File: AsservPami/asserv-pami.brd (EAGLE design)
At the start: 69.5 x 81.3 mm, 31 parts, among them IC1 NUCLEO-G431KB, IC2 7805TV

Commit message: ajout BAU et Voltmetre + label
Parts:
- added BAU, VOLTMETRE: 22-23-2021, con-molex:22-23-2021
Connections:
- new net N$7: BATTERIE.2, BAU.1
- net GND: now also VOLTMETRE.1
- net VIN: now also BAU.2, VOLTMETRE.2; no longer BATTERIE.2
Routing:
- net VIN: track 57.2 -> 66.7 mm
- net N$7: track 0.00 -> 8.67 mm
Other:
- board text added: "Alim"
- board text added: "BAU"
- board text added: "Codeur1"
- board text added: "Codeur2"
- board text added: "Couleur"
- board text added: "GPIO1"
- board text added: "GPIO2"
- board text added: "I2C"
- board text added: "Moteur1"
- board text added: "Moteur2"
- board text added: "Servo1"
- board text added: "Servo2"
- board text added: "StepUp"
- board text added: "Tirette"
- board text added: "UART"
- board text added: "USB DEBUG"
- board text added: "Volt"
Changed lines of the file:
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@@
 <hole x="29.21" y="3.81" drill="3"/>
 <hole x="12.7" y="74.93" drill="3"/>
+<text x="63.5" y="57.15" size="1.016" layer="1">Alim</text>
+<text x="54.61" y="57.15" size="1.016" layer="1">BAU</text>
+<text x="46.99" y="57.15" size="1.016" layer="1">Volt</text>
+<text x="64.77" y="50.8" size="1.016" layer="1" rot="R90">Codeur1</text>
+<text x="55.88" y="50.8" size="1.016" layer="1" rot="R90">Codeur2</text>
+<text x="54.61" y="36.83" size="1.016" layer="1">StepUp</text>
+<text x="55.88" y="2.54" size="1.016" layer="1">Moteur1</text>
+<text x="36.83" y="2.54" size="1.016" layer="1">Moteur2</text>
+<text x="13.97" y="22.86" size="1.016" layer="1" rot="R90">Tirette</text>
+<text x="13.97" y="15.24" size="1.016" layer="1" rot="R90">Couleur</text>
+<text x="13.97" y="8.89" size="1.016" layer="1" rot="R90">GPIO1</text>
+<text x="13.97" y="2.54" size="1.016" layer="1" rot="R90">GPIO2</text>
+<text x="10.16" y="38.1" size="1.016" layer="1" rot="R180">UART</text>
+<text x="22.86" y="40.64" size="1.016" layer="1" rot="R270">Servo1</text>
+<text x="22.86" y="34.29" size="1.016" layer="1" rot="R270">Servo2</text>
+<text x="19.05" y="53.34" size="1.016" layer="1">I2C</text>
+<text x="54.61" y="78.74" size="1.016" layer="1">USB DEBUG</text>
 </plain>
 <attributes>
@@
 <attribute name="VALUE" x="53.848" y="39.116" size="1.27" layer="27" ratio="10"/>
 </element>
+<element name="BAU" library="con-molex" library_urn="urn:adsk.eagle:library:165" package="22-23-2021" value="22-23-2021" x="57.15" y="60.96" smashed="yes" rot="R90">
+<attribute name="MF" value="MOLEX" x="45.72" y="53.34" size="1.778" layer="27" rot="R90" display="off"/>
+<attribute name="MPN" value="22-23-2021" x="45.72" y="53.34" size="1.778" layer="27" rot="R90" display="off"/>
+<attribute name="NAME" x="53.34" y="58.42" size="1.016" layer="25" ratio="10" rot="R90"/>
+<attribute name="OC_FARNELL" value="1462926" x="45.72" y="53.34" size="1.778" layer="27" rot="R90" display="off"/>
+<attribute name="OC_NEWARK" value="25C3832" x="45.72" y="53.34" size="1.778" layer="27" rot="R90" display="off"/>
+<attribute name="VALUE" x="62.23" y="58.42" size="1.016" layer="27" ratio="10" rot="R90"/>
+</element>
+<element name="VOLTMETRE" library="con-molex" library_urn="urn:adsk.eagle:library:165" package="22-23-2021" value="22-23-2021" x="49.53" y="60.96" smashed="yes" rot="R90">
+<attribute name="MF" value="MOLEX" x="38.1" y="53.34" size="1.778" layer="27" rot="R90" display="off"/>
+<attribute name="MPN" value="22-23-2021" x="38.1" y="53.34" size="1.778" layer="27" rot="R90" display="off"/>
+<attribute name="NAME" x="45.72" y="58.42" size="1.016" layer="25" ratio="10" rot="R90"/>
+<attribute name="OC_FARNELL" value="1462926" x="38.1" y="53.34" size="1.778" layer="27" rot="R90" display="off"/>
+<attribute name="OC_NEWARK" value="25C3832" x="38.1" y="53.34" size="1.778" layer="27" rot="R90" display="off"/>
+<attribute name="VALUE" x="54.61" y="58.42" size="1.016" layer="27" ratio="10" rot="R90"/>
+</element>
 </elements>
 <signals>
@@
 <contactref element="IC2" pad="2"/>
 <contactref element="C2" pad="2"/>
-<contactref element="BATTERIE" pad="1"/>
 <contactref element="POLOLU-MP6550-1-2" pad="5"/>
 <contactref element="POLOLU-MP6550-2-2" pad="5"/>
@@
 <wire x1="57.15" y1="68.58" x2="57.15" y2="67.31" width="1.016" layer="1"/>
 <contactref element="C3" pad="1"/>
+<contactref element="BATTERIE" pad="1"/>
+<contactref element="VOLTMETRE" pad="1"/>
 </signal>
 <signal name="N$1">
@@
 </signal>
 <signal name="VIN">
-<contactref element="BATTERIE" pad="2"/>
 <contactref element="C1" pad="1"/>
 <contactref element="IC2" pad="1"/>
 <contactref element="POLOLU-U3V40F12" pad="4"/>
 <contactref element="POLOLU-U3V40F12" pad="5"/>
-<wire x1="54.61" y1="67.31" x2="54.61" y2="63.5" width="1.016" layer="16"/>
-<wire x1="54.61" y1="63.5" x2="55.88" y2="62.23" width="1.016" layer="16"/>
 <wire x1="60.96" y1="39.37" x2="58.42" y2="39.37" width="1.016" layer="16"/>
-<wire x1="55.88" y1="62.23" x2="64.77" y2="62.23" width="1.016" layer="16"/>
-<wire x1="64.77" y1="62.23" x2="66.04" y2="62.23" width="1.016" layer="16"/>
-<wire x1="66.04" y1="62.23" x2="67.31" y2="60.96" width="1.016" layer="16"/>
 <wire x1="67.31" y1="60.96" x2="67.31" y2="43.18" width="1.016" layer="16"/>
 <wire x1="62.23" y1="43.18" x2="60.96" y2="41.91" width="1.016" layer="16"/>
@@
 <contactref element="C3" pad="2"/>
 <wire x1="58.42" y1="39.37" x2="58.42" y2="41.91" width="1.016" layer="16"/>
+<contactref element="BAU" pad="2"/>
+<wire x1="57.15" y1="62.23" x2="59.69" y2="62.23" width="1" layer="16"/>
+<wire x1="59.69" y1="62.23" x2="62.23" y2="64.77" width="1" layer="16"/>
+<wire x1="62.23" y1="64.77" x2="66.04" y2="64.77" width="1" layer="16"/>
+<wire x1="66.04" y1="64.77" x2="67.31" y2="63.5" width="1" layer="16"/>
+<wire x1="67.31" y1="63.5" x2="67.31" y2="60.96" width="1" layer="16"/>
+<contactref element="VOLTMETRE" pad="2"/>
+<wire x1="57.15" y1="62.23" x2="54.61" y2="62.23" width="1" layer="16"/>
+<wire x1="54.61" y1="62.23" x2="49.53" y2="62.23" width="1" layer="16"/>
+<wire x1="54.61" y1="67.31" x2="54.61" y2="62.23" width="1" layer="16"/>
 </signal>
 <signal name="SDA">
@@
 <wire x1="8.89" y1="38.1" x2="8.89" y2="35.56" width="1.016" layer="16"/>
 </signal>
+<signal name="N$7">
+<contactref element="BATTERIE" pad="2"/>
+<contactref element="BAU" pad="1"/>
+<wire x1="57.15" y1="59.69" x2="59.69" y2="59.69" width="1" layer="16"/>
+<wire x1="59.69" y1="59.69" x2="62.23" y2="62.23" width="1" layer="16"/>
+<wire x1="62.23" y1="62.23" x2="64.77" y2="62.23" width="1" layer="16"/>
+</signal>
 </signals>

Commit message: for impression
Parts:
- moved TIRETTE 6.35 mm to (8.89, 31.8)
- moved UART 6.35 mm to (8.89, 40.6)
- moved COULEUR 5.08 mm to (8.89, 22.9)
- moved GPIO1 2.54 mm to (8.89, 14.0)
- moved C1 2.54 mm to (52.1, 73.7)
- moved I2C 1.27 mm to (19.1, 44.5)
- moved SERVO2 1.27 mm to (21.6, 30.5)
- moved USB-DEBUG 1.27 mm to (53.3, 78.7)
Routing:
- net N$6: track 41.9 -> 35.3 mm
- net N$5: track 41.7 -> 36.8 mm
- net TIRETTE: track 62.5 -> 58.1 mm
- net COULEUR: track 66.4 -> 63.9 mm
- net SERVO1: track 35.1 -> 36.6 mm
- net SCL: track 29.0 -> 30.3 mm
- net USB-D+: track 44.7 -> 43.4 mm
- net SERVO2: track 39.7 -> 40.9 mm
- net SDA: track 35.9 -> 37.1 mm
- net GND: track 1.27 -> 0.00 mm
- net VIN: track 66.7 -> 65.6 mm
- net GPIO1: track 69.9 -> 69.2 mm
- net 5V: track 178.1 -> 178.6 mm

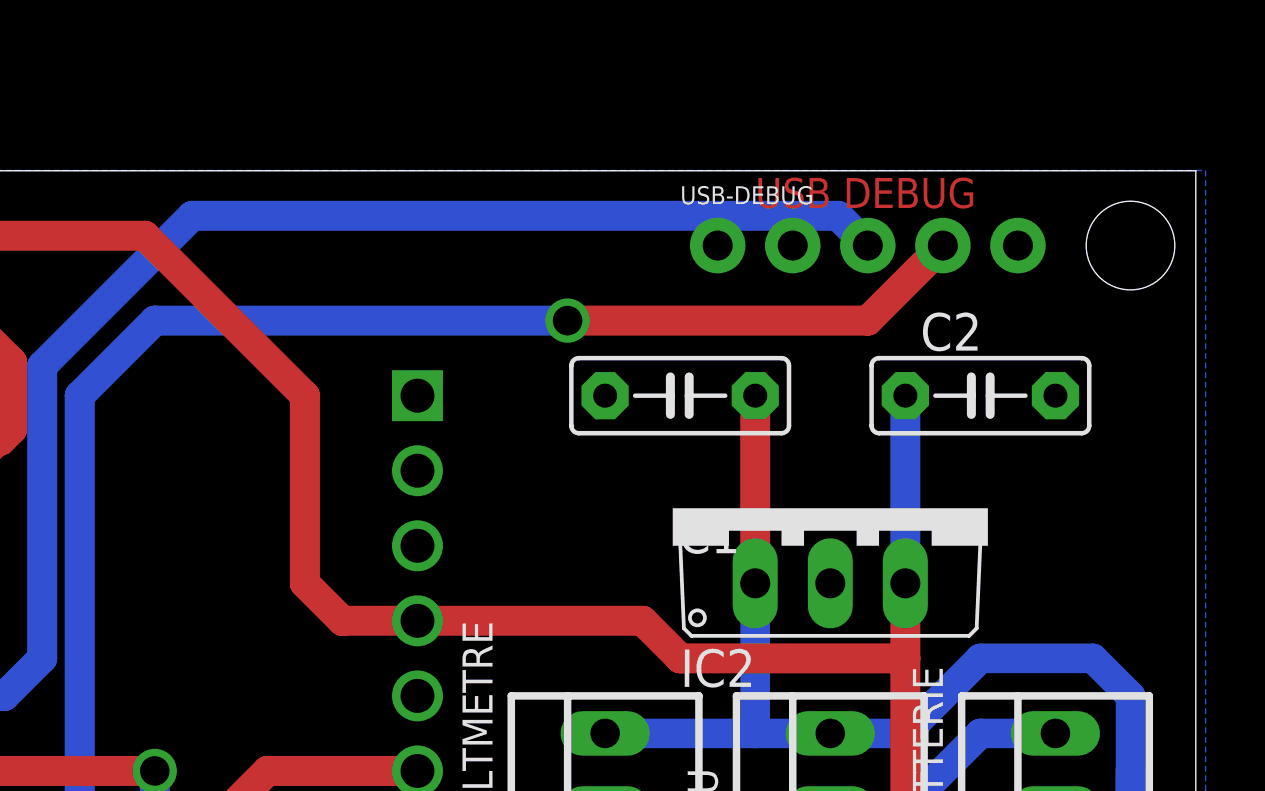
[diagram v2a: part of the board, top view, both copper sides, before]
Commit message: fix court circuit
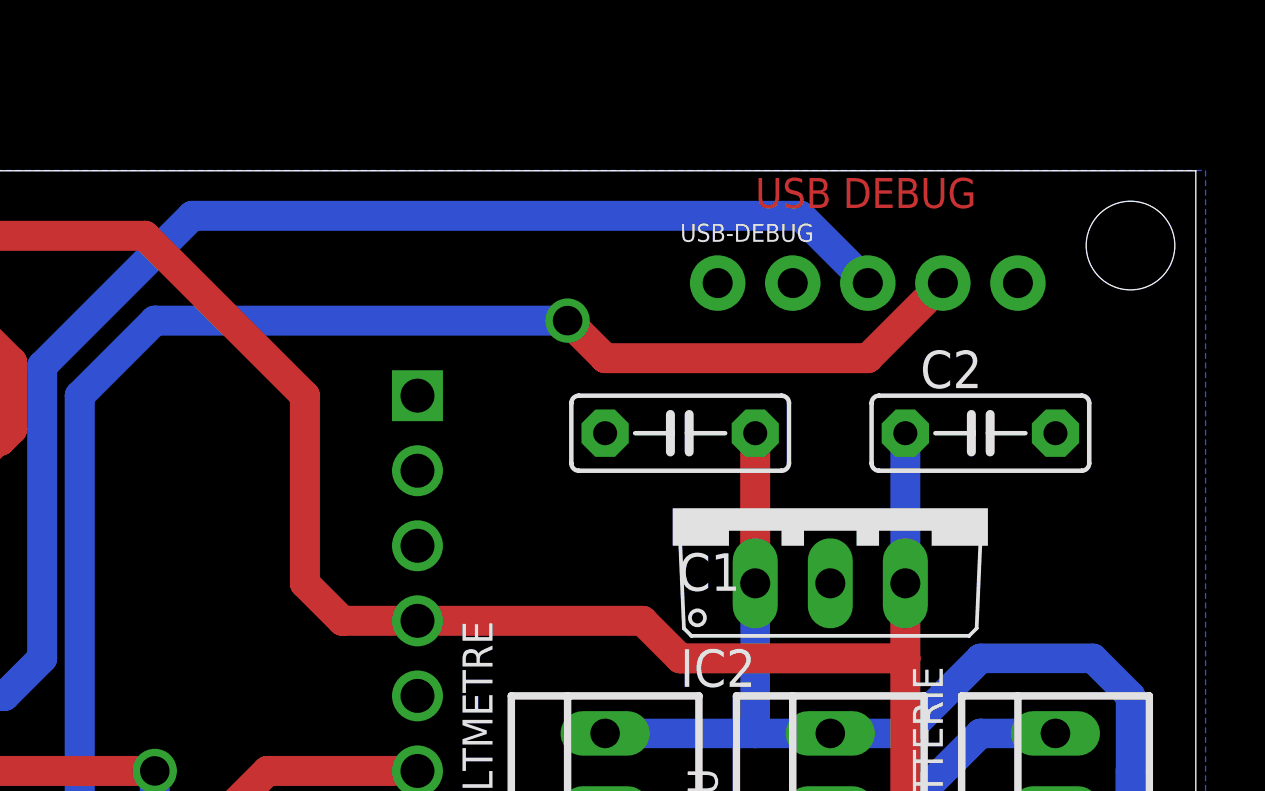
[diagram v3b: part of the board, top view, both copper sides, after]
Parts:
- moved C1 1.27 mm to (52.1, 72.4)
- moved C2 1.27 mm to (62.2, 72.4)
- moved USB-DEBUG 1.27 mm to (53.3, 77.5)
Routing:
- net 5V: track 178.6 -> 177.3 mm
- net VIN: track 65.6 -> 64.3 mm
- net USB-D-: track 64.9 -> 65.4 mm
- net USB-D+: track 43.4 -> 43.9 mm
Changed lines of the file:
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@@
 <attribute name="VALUE" x="69.85" y="58.42" size="1.016" layer="27" ratio="10" rot="R90"/>
 </element>
-<element name="C1" library="capacitor-wima" library_urn="urn:adsk.eagle:library:116" package="C5B2.5" value="0.33uF" x="52.07" y="73.66" smashed="yes" rot="R180">
-<attribute name="NAME" x="54.102" y="69.596" size="1.27" layer="25" ratio="10" rot="R180"/>
-<attribute name="VALUE" x="54.102" y="76.454" size="1.27" layer="27" ratio="10" rot="R180"/>
-</element>
-<element name="C2" library="capacitor-wima" library_urn="urn:adsk.eagle:library:116" package="C5B2.5" value="0.1uF" x="62.23" y="73.66" smashed="yes">
-<attribute name="NAME" x="60.198" y="75.184" size="1.27" layer="25" ratio="10"/>
-<attribute name="VALUE" x="60.198" y="70.866" size="1.27" layer="27" ratio="10"/>
+<element name="C1" library="capacitor-wima" library_urn="urn:adsk.eagle:library:116" package="C5B2.5" value="0.33uF" x="52.07" y="72.39" smashed="yes" rot="R180">
+<attribute name="NAME" x="54.102" y="68.326" size="1.27" layer="25" ratio="10" rot="R180"/>
+<attribute name="VALUE" x="54.102" y="75.184" size="1.27" layer="27" ratio="10" rot="R180"/>
+</element>
+<element name="C2" library="capacitor-wima" library_urn="urn:adsk.eagle:library:116" package="C5B2.5" value="0.1uF" x="62.23" y="72.39" smashed="yes">
+<attribute name="NAME" x="60.198" y="73.914" size="1.27" layer="25" ratio="10"/>
+<attribute name="VALUE" x="60.198" y="69.596" size="1.27" layer="27" ratio="10"/>
 </element>
 <element name="CODEUR1" library="SparkFun-Connectors" library_urn="urn:adsk.eagle:library:513" package="1X04" package3d_urn="urn:adsk.eagle:package:38085/2" value="" x="62.23" y="46.99" smashed="yes" rot="R90">
@@
 <attribute name="VALUE" x="46.99" y="27.432" size="0.6096" layer="27" font="vector" ratio="20" rot="R180"/>
 </element>
-<element name="USB-DEBUG" library="SparkFun-Connectors" library_urn="urn:adsk.eagle:library:513" package="1X05_NO_SILK" package3d_urn="urn:adsk.eagle:package:38108/2" value="" x="53.34" y="78.74" smashed="yes">
-<attribute name="NAME" x="52.07" y="80.137" size="0.6096" layer="25" font="vector" ratio="20"/>
-<attribute name="VALUE" x="52.07" y="76.708" size="0.6096" layer="27" font="vector" ratio="20"/>
+<element name="USB-DEBUG" library="SparkFun-Connectors" library_urn="urn:adsk.eagle:library:513" package="1X05_NO_SILK" package3d_urn="urn:adsk.eagle:package:38108/2" value="" x="53.34" y="77.47" smashed="yes">
+<attribute name="NAME" x="52.07" y="78.867" size="0.6096" layer="25" font="vector" ratio="20"/>
+<attribute name="VALUE" x="52.07" y="75.438" size="0.6096" layer="27" font="vector" ratio="20"/>
 </element>
 <element name="R-5K" library="rcl" library_urn="urn:adsk.eagle:library:334" package="0204/7" package3d_urn="urn:adsk.eagle:package:23498/1" value="" x="27.94" y="15.24" smashed="yes" rot="R90">
@@
 <contactref element="IC1" pad="5"/>
 <contactref element="USB-DEBUG" pad="3"/>
-<wire x1="58.42" y1="78.74" x2="57.414" y2="79.746" width="1.016" layer="16"/>
-<wire x1="57.414" y1="79.746" x2="35.56" y2="79.746" width="1.016" layer="16"/>
+<wire x1="58.42" y1="77.47" x2="56.144" y2="79.746" width="1.016" layer="16"/>
+<wire x1="56.144" y1="79.746" x2="35.56" y2="79.746" width="1.016" layer="16"/>
 <wire x1="35.56" y1="79.746" x2="30.48" y2="74.666" width="1.016" layer="16"/>
 <wire x1="30.48" y1="74.666" x2="30.48" y2="64.77" width="1.016" layer="16"/>
@@
 <wire x1="30.48" y1="43.18" x2="27.94" y2="43.18" width="1.016" layer="16"/>
 <via x="48.26" y="76.2" extent="1-16" drill="1"/>
-<wire x1="58.42" y1="76.2" x2="60.96" y2="78.74" width="1.016" layer="1"/>
-<wire x1="48.26" y1="76.2" x2="58.42" y2="76.2" width="1.016" layer="1"/>
+<wire x1="58.42" y1="74.93" x2="60.96" y2="77.47" width="1.016" layer="1"/>
+<wire x1="48.26" y1="76.2" x2="49.53" y2="74.93" width="1.016" layer="1"/>
+<wire x1="58.42" y1="74.93" x2="49.53" y2="74.93" width="1.016" layer="1"/>
 </signal>
 <signal name="MPC-ON">
@@
 <contactref element="SERVO1" pad="2"/>
 <wire x1="22.86" y1="27.94" x2="19.05" y2="27.94" width="1.016" layer="16"/>
-<wire x1="59.69" y1="73.66" x2="59.69" y2="67.31" width="1.016" layer="16"/>
+<wire x1="59.69" y1="72.39" x2="59.69" y2="67.31" width="1.016" layer="16"/>
 <wire x1="53.34" y1="52.07" x2="59.69" y2="52.07" width="1.016" layer="16"/>
 <wire x1="59.69" y1="52.07" x2="62.23" y2="52.07" width="1.016" layer="16"/>
@@
 <wire x1="60.96" y1="41.91" x2="60.96" y2="39.37" width="1.016" layer="16"/>
 <wire x1="67.31" y1="43.18" x2="62.23" y2="43.18" width="1.016" layer="16"/>
-<wire x1="54.61" y1="67.31" x2="54.61" y2="73.66" width="1.016" layer="1"/>
+<wire x1="54.61" y1="67.31" x2="54.61" y2="72.39" width="1.016" layer="1"/>
 <contactref element="C3" pad="2"/>
 <wire x1="58.42" y1="39.37" x2="58.42" y2="41.91" width="1.016" layer="16"/>

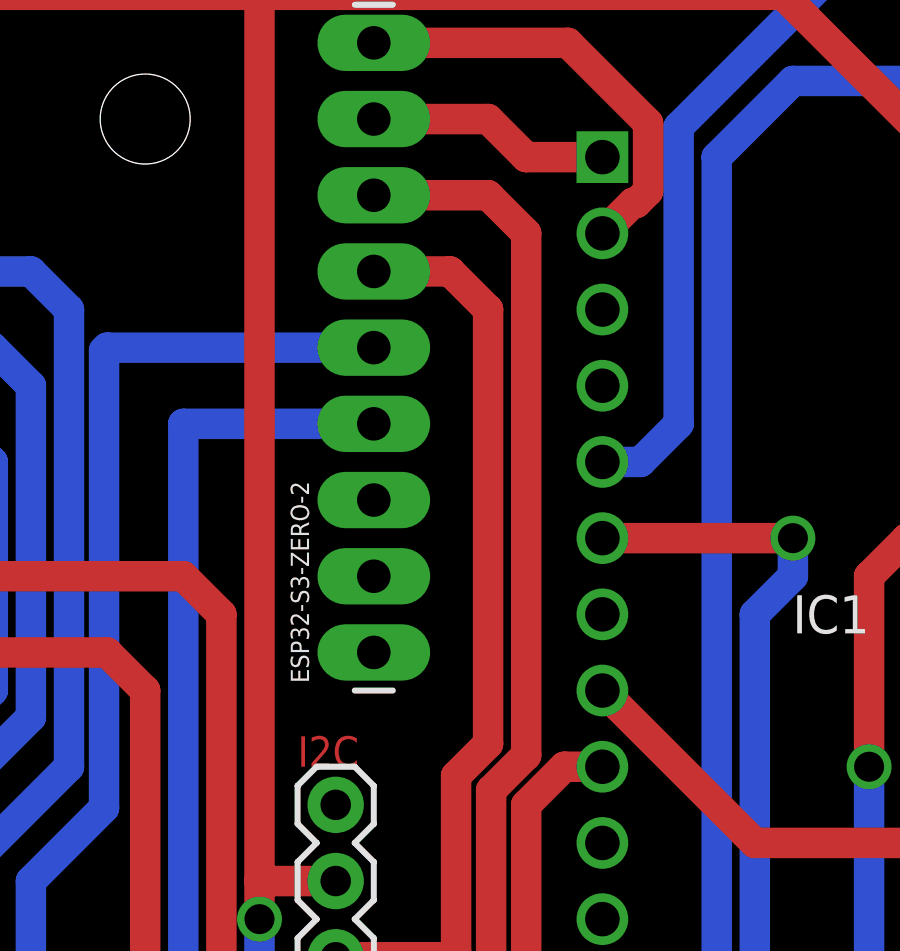
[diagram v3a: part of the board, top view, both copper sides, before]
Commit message: fix i2c
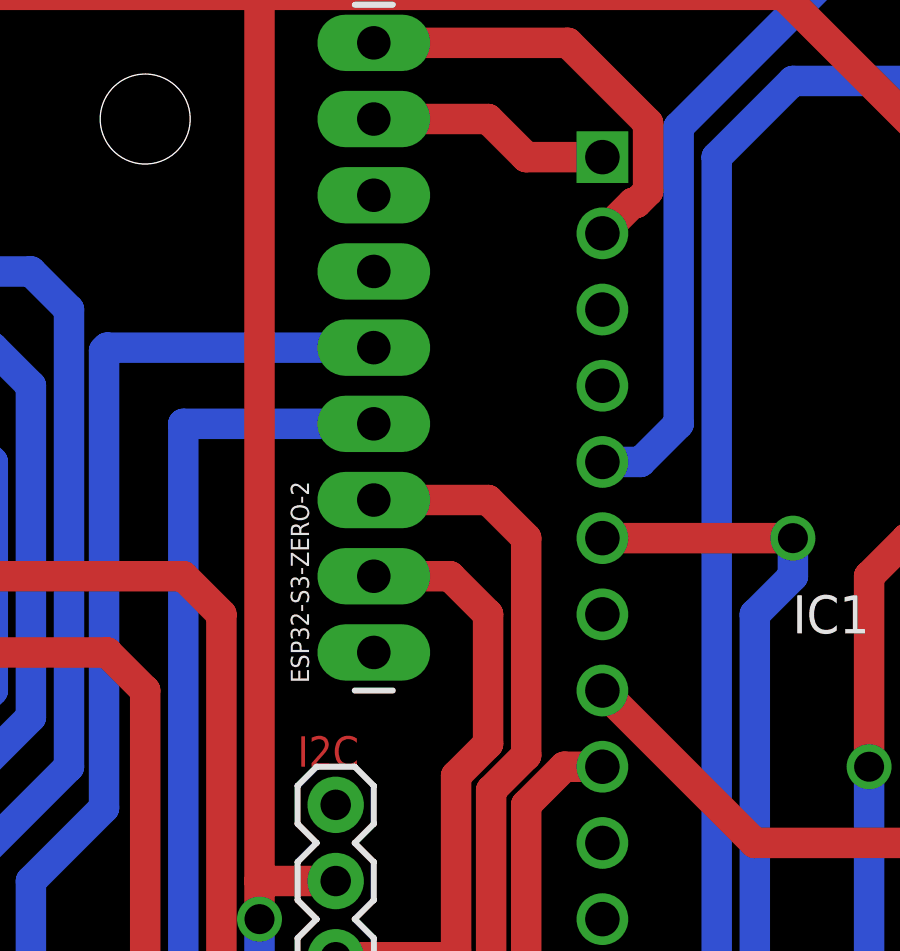
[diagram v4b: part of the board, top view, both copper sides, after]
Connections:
- net SCL: now also ESP32-S3-ZERO-2.2; no longer ESP32-S3-ZERO-2.6
- net SDA: now also ESP32-S3-ZERO-2.3; no longer ESP32-S3-ZERO-2.7
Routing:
- net SDA: track 37.1 -> 27.0 mm
- net SCL: track 30.3 -> 20.1 mm
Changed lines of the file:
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@@
 </signal>
 <signal name="SDA">
-<contactref element="ESP32-S3-ZERO-2" pad="7"/>
 <contactref element="I2C" pad="1"/>
 <wire x1="19.05" y1="44.45" x2="22.86" y2="44.45" width="1.016" layer="1"/>
 <wire x1="22.86" y1="44.45" x2="24.2316" y2="45.8216" width="1.016" layer="1"/>
 <wire x1="24.2316" y1="45.8216" x2="24.2316" y2="52.55396875" width="1.016" layer="1"/>
-<wire x1="25.4" y1="53.72236875" x2="25.4" y2="71.12" width="1.016" layer="1"/>
+<wire x1="25.4" y1="53.72236875" x2="25.4" y2="60.96" width="1.016" layer="1"/>
 <wire x1="24.2316" y1="52.55396875" x2="25.4" y2="53.72236875" width="1.016" layer="1"/>
-<wire x1="25.4" y1="71.12" x2="24.13" y2="72.39" width="1.016" layer="1"/>
-<wire x1="24.13" y1="72.39" x2="20.32" y2="72.39" width="1.016" layer="1"/>
+<wire x1="25.4" y1="60.96" x2="24.13" y2="62.23" width="1.016" layer="1"/>
+<contactref element="ESP32-S3-ZERO-2" pad="3"/>
+<wire x1="24.13" y1="62.23" x2="20.32" y2="62.23" width="1.016" layer="1"/>
 </signal>
 <signal name="SCL">
-<contactref element="ESP32-S3-ZERO-2" pad="6"/>
 <contactref element="I2C" pad="2"/>
 <wire x1="19.05" y1="46.99" x2="22.86" y2="46.99" width="1.016" layer="1"/>
 <wire x1="22.86" y1="46.99" x2="23.0632" y2="47.1932" width="1.016" layer="1"/>
 <wire x1="23.0632" y1="47.1932" x2="23.0632" y2="53.0379375" width="1.016" layer="1"/>
-<wire x1="24.13" y1="54.1047375" x2="24.13" y2="68.58" width="1.016" layer="1"/>
+<wire x1="24.13" y1="54.1047375" x2="24.13" y2="58.42" width="1.016" layer="1"/>
 <wire x1="23.0632" y1="53.0379375" x2="24.13" y2="54.1047375" width="1.016" layer="1"/>
-<wire x1="24.13" y1="68.58" x2="22.86" y2="69.85" width="1.016" layer="1"/>
-<wire x1="22.86" y1="69.85" x2="20.32" y2="69.85" width="1.016" layer="1"/>
+<wire x1="24.13" y1="58.42" x2="22.86" y2="59.69" width="1.016" layer="1"/>
+<contactref element="ESP32-S3-ZERO-2" pad="2"/>
+<wire x1="22.86" y1="59.69" x2="20.32" y2="59.69" width="1.016" layer="1"/>
 </signal>
 <signal name="TIRETTE">
